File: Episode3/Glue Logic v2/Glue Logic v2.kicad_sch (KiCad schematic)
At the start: 8 parts, among them J1 5V DC

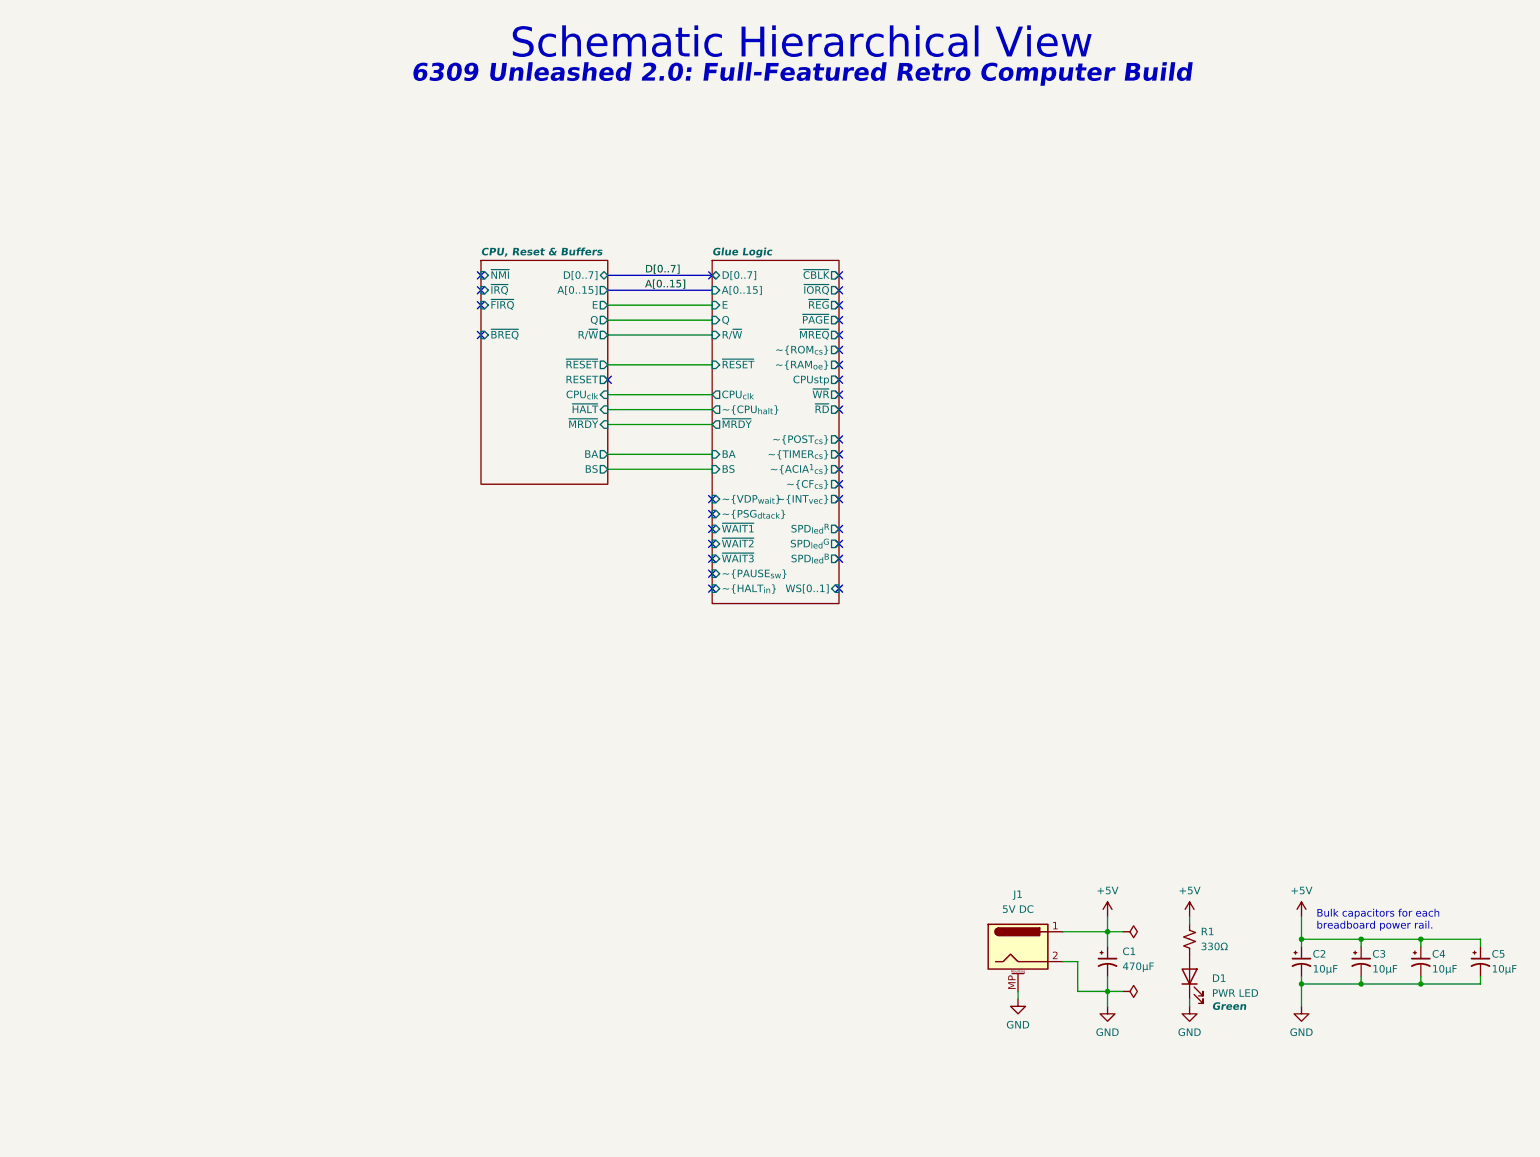
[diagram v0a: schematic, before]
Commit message: changed strategy and simplified things
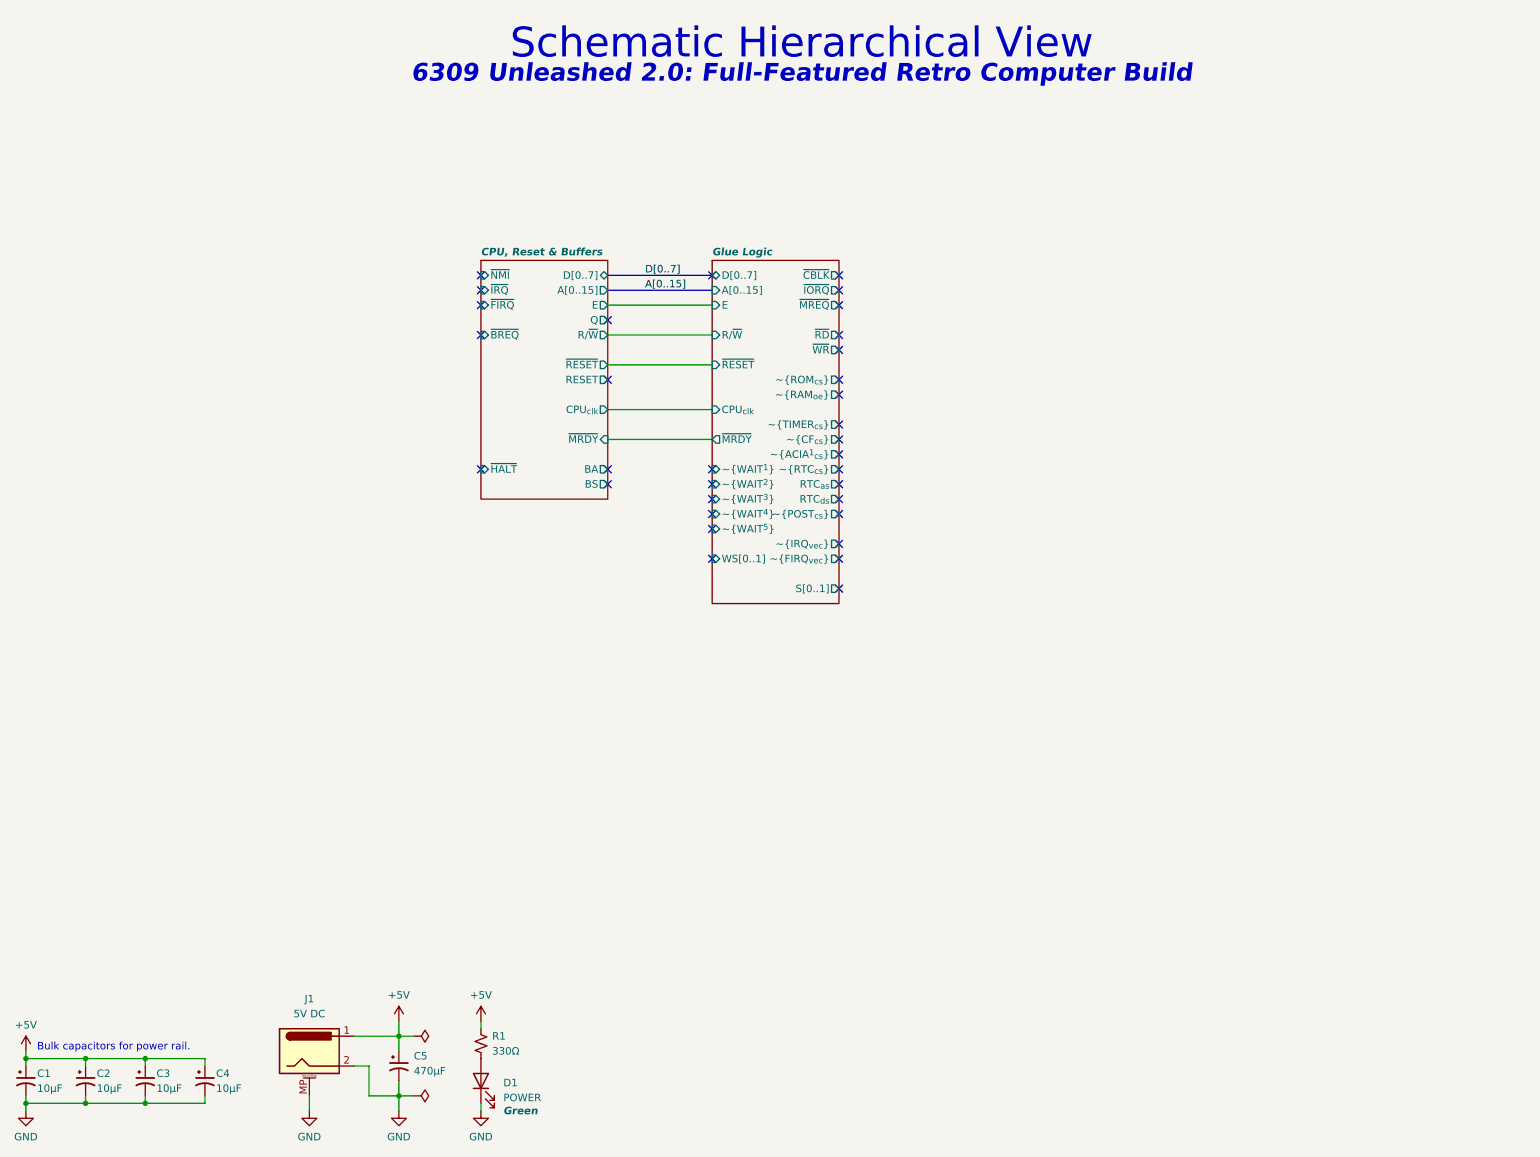
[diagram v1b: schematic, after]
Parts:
- D1: value PWR LED -> POWER
- renumbered C2 to C1, C3 to C2, C4 to C3, C5 to C4, C1 to C5
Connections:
- no-connect marks 32 -> 33
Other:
- sheet Glue Logic ports: added RTC_{as}, RTC_{ds}, S[0..1], ~{FIRQ_{vec}}, ~{IRQ_{vec}}, ~{RTC_{cs}}, ~{WAIT^{1}}, ~{WAIT^{2}}, ~{WAIT^{3}}, ~{WAIT^{4}}, ~{WAIT^{5}}; removed BA, BS, CPUstp, Q, SPD_{led}^{B}, SPD_{led}^{G}, SPD_{led}^{R}, ~{CPU_{halt}}, ~{HALT_{in}}, ~{INT_{vec}}, ~{PAGE}, ~{PAUSE_{sw}}, ~{PSG_{dtack}}, ~{REG}, ~{VDP_{wait}}, ~{WAIT1}, ~{WAIT2}, ~{WAIT3}
- note added: "Bulk capacitors for power rail."
- note removed: "Bulk capacitors for each breadboard power rail."
- moved on the sheet: C1, C2, C3, C4, C5, D1, J1, R1

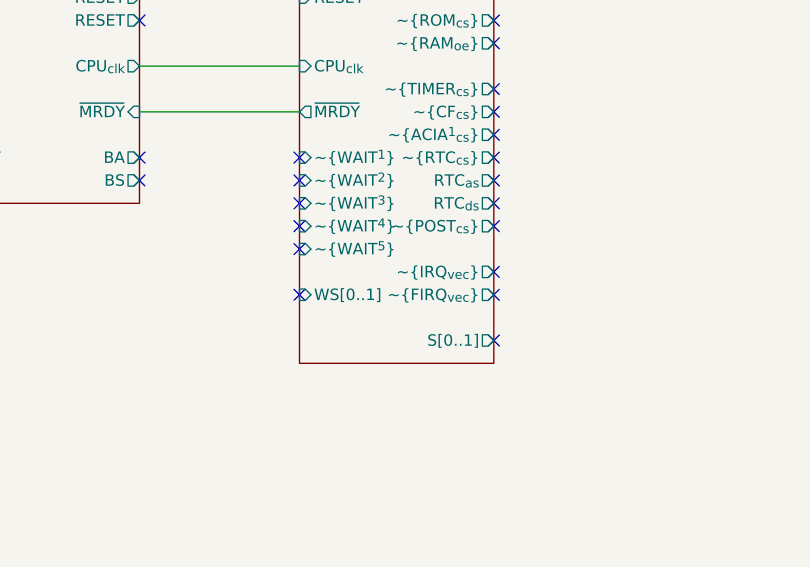
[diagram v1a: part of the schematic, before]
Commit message: Massive changes to the PLD code (tested) - Minor changes to the Schematic
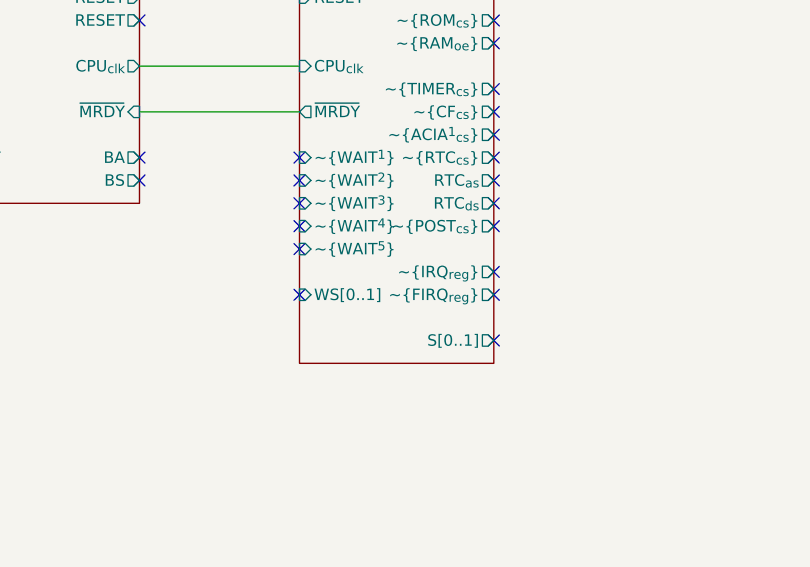
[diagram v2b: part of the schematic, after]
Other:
- sheet Glue Logic ports: added ~{FIRQ_{reg}}, ~{IRQ_{reg}}; removed ~{FIRQ_{vec}}, ~{IRQ_{vec}}
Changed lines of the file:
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@@
 			)
 		)
-		(pin "~{IRQ_{vec}}" output
+		(pin "~{IRQ_{reg}}" output
 			(at 151.13 104.14 0)
 			(effects
@@
 			)
 		)
-		(pin "~{FIRQ_{vec}}" output
+		(pin "~{FIRQ_{reg}}" output
 			(at 151.13 106.68 0)
 			(effects
